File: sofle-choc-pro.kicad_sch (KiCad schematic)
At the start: 198 parts, among them J1 Connector, USB-TYPE-C-16P, J2 Connector, USB-TYPE-C-16P, J3 OLED 128x32 / nice!view, SW1 BOOT, SW10 F0, SW11 F1, SW12 F2, SW13 F3, SW14 F4, SW15 F5, SW16 F6 Choc/EC11, SW2 RESET, SW20 N0, SW21 N1, SW22 N2, SW23 N3, SW24 N4, SW25 N5, SW30 T0, SW31 T1, SW32 T2, SW33 T3, SW34 T4, SW35 T5, SW40 H0, SW41 H1, SW42 H2, SW43 H3, SW44 H4, SW45 H5, SW50 B0, SW51 B1, SW52 B2, SW53 B3, SW54 B4, SW55 B5, SW60 TH0, SW61 TH1, SW62 TH2, SW63 TH3, SW64 TH4, SW65 TH5 Choc/EC11, U1 RP2040, U2 USBLC6-2P6, U3 W25Q128JVPIQ, U4 USBLC6-2P6, U5 AP2112K-3.3, U6 SN74LV1T34DBVR, X1 ABM8-272-T3

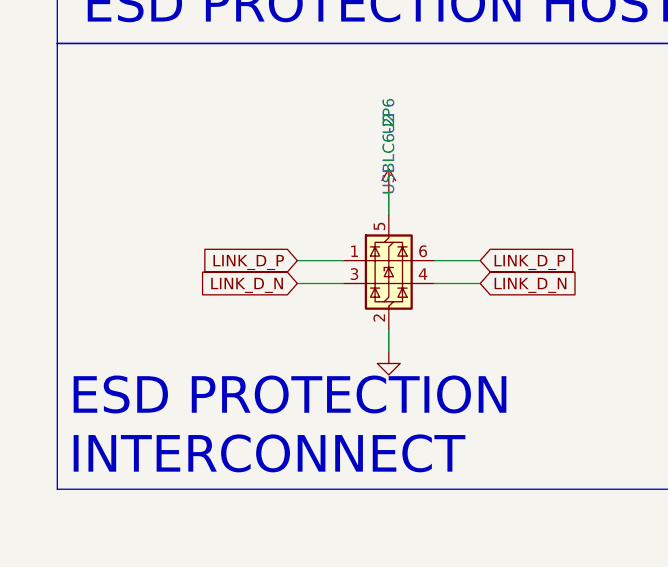
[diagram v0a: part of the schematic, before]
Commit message: fix(pcb): drop the dead link d- pad and exempt the esd fan-out
The link between halves is one-wire serial, so D- stops at the ESD array.
Both of its pads carried the net, which left KiCad asking for copper between
two pins the chip already joins inside. Now only the pad the connector
reaches is wired, and the other is a no-connect.

- U2 pin 3 disconnected in the schematic and on the board: four fewer
  unconnected items, and no more phantom pad-to-pad link
- D+/D- spacing rule now skips U4's courtyard as well as J1's and U1's,
  since the ESD array's two data pins sit 2.3 mm apart and set the gap

Also carries the USB and link routing done in KiCad since the last commit.

ERC 0 errors. DRC 0 errors, 0 parity issues. One skew flag remains on the
host pair (0.23 mm), to even out once that pair is finished.
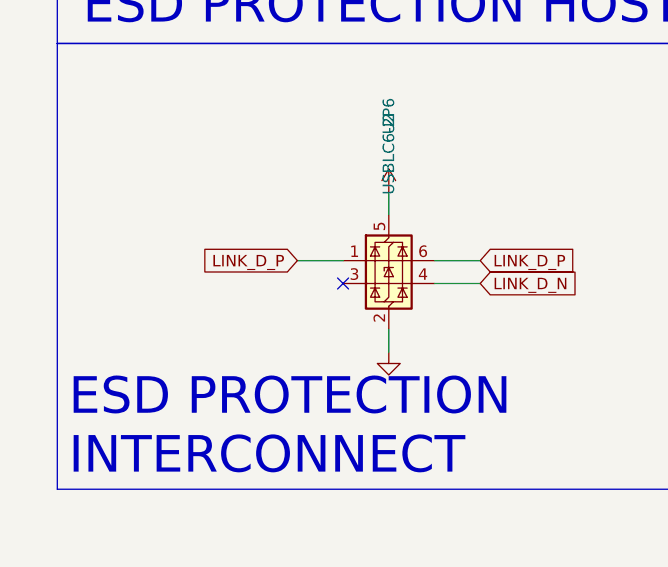
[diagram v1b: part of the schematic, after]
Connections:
- net LINK_D_N: no longer U2.3 (I/O2)
- no-connect marks 14 -> 15
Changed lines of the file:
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@@
 	(wire
 		(pts
-			(xy 45.72 269.24) (xy 40.64 269.24)
-		)
-		(stroke
-			(width 0)
-			(type default)
-		)
-	)
-	(wire
-		(pts
 			(xy 546.1 162.56) (xy 543.56 162.56)
 		)
@@
 		)
 	)
-	(global_label "LINK_D_N"
-		(shape input)
-		(at 40.64 269.24 180)
-		(effects
-			(font
-				(size 1.27 1.27)
-			)
-			(justify right)
-		)
-		(property "Intersheetrefs" "${INTERSHEET_REFS}"
-			(at 40.64 269.24 0)
-			(hide yes)
-			(show_name no)
-			(do_not_autoplace no)
-			(effects
-				(font
-					(size 1.27 1.27)
-				)
-			)
-		)
-	)
 	(global_label "LED_D23"
 		(shape bidirectional)
@@
 	)
 	(embedded_fonts no)
+	(no_connect
+		(at 45.72 269.24)
+	)
 )

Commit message: feat(pcb): route all power through the inner planes
Every power and ground pad is now connected, through a short stub to a
via beside the pad into the In1 and In2 planes, so the outer layers stay
free for signals.

- USB pair joined through U4: U2 and U4 use a project SOT-563 footprint
  that declares pins 1/6 and 3/4 as bonded, as ST's USBLC6-2 datasheet
  routes them, so D+/D- flow through the package
- VBUS runs 0.5 mm straight from J1 to F1; the D1 to U4 +5V trunk that
  blocked it is gone, and F1 to D1 widens to 0.5 mm
- +5V vias at D1/C18, U4, U2, U5, C20, F2, U6/C30 and every LED; each LED
  cap also gets a GND stitching via
- LINK_VBUS runs from J2 to F2, J2's two VBUS pads joined by an In1 strip;
  LINK_VBUS joins the Power5V class
- R10 moves beside the VBUS run so sense stays short; GP13 exits by a via
- J3 pin 3 takes +3.3V from an In1 branch; JP1's +3.3V logic tie runs
  0.2 mm on F.Cu down the right edge
- Two cap vias that sat within 0.1 mm of their pads get short stubs

Checks: DRC 0 errors, parity 0, ERC 0; nothing unconnected on power or
GND (179 signal items left, the GP13 via dangles until GP13 is routed).
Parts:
- U2, U4: footprint Package_TO_SOT_SMD:SOT-563 -> my-soffle:SOT-563_USBLC6-2P6
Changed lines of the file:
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@@
 			)
 		)
-		(property "Footprint" "Package_TO_SOT_SMD:SOT-563"
+		(property "Footprint" "my-soffle:SOT-563_USBLC6-2P6"
 			(at 60.96 217.17 0)
 			(hide yes)
@@
 			)
 		)
-		(property "Footprint" "Package_TO_SOT_SMD:SOT-563"
+		(property "Footprint" "my-soffle:SOT-563_USBLC6-2P6"
 			(at 60.96 266.7 0)
 			(hide yes)

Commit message: feat(pcb): start the led chain at the encoders and route columns 4-5
The LED data chain now runs R15, LED16, LED65, the thumbs, column 5 up
and column 4 down, so it no longer detours across column 5 to reach the
upper encoder. Columns 4 and 5 are routed by hand on the new order.

- Chain order picked by scoring every order on pad-to-pad length and
  crossings: 663 mm instead of 719 mm, no hop crosses a foreign key
  cell except LED63 to LED55 around SW2
- Only LED_D0 to LED_D8 were reassigned (9 LEDs); the routed tail from
  LED62 on is unchanged
- LED_D3 to LED_D14 routed, plus reworked GP22, GP24 and matrix nets

ERC: 0 errors. DRC: 0 errors, 0 parity, 29 unconnected. Known issues
to fix next: LED35/45/55 GND pads sealed off by the new data routes,
8 data vias touching their pads, a dangling GP22 via.
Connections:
- net LED_D0: now also LED16.2 (DIN); no longer LED65.2 (DIN)
- net LED_D1: now also LED16.4 (DOUT), LED65.2 (DIN); no longer LED64.2 (DIN), LED65.4 (DOUT)
- net LED_D2: now also LED64.2 (DIN), LED65.4 (DOUT); no longer LED63.2 (DIN), LED64.4 (DOUT)
- net LED_D3: now also LED63.2 (DIN), LED64.4 (DOUT); no longer LED55.2 (DIN), LED63.4 (DOUT)
- net LED_D4: now also LED55.2 (DIN), LED63.4 (DOUT); no longer LED45.2 (DIN), LED55.4 (DOUT)
- net LED_D5: now also LED45.2 (DIN), LED55.4 (DOUT); no longer LED35.2 (DIN), LED45.4 (DOUT)
- net LED_D6: now also LED35.2 (DIN), LED45.4 (DOUT); no longer LED25.2 (DIN), LED35.4 (DOUT)
- net LED_D7: now also LED25.2 (DIN), LED35.4 (DOUT); no longer LED15.2 (DIN), LED25.4 (DOUT)
- net LED_D8: now also LED15.2 (DIN), LED25.4 (DOUT); no longer LED15.4 (DOUT), LED16.2 (DIN)
- net LED_D9: now also LED15.4 (DOUT); no longer LED16.4 (DOUT)
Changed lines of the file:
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@@
 		)
 	)
-	(global_label "LED_D4"
+	(global_label "LED_D5"
 		(shape bidirectional)
 		(at 576.58 237.49 0)
@@
 		)
 	)
-	(global_label "LED_D9"
+	(global_label "LED_D1"
 		(shape bidirectional)
 		(at 444.5 273.05 0)
@@
 		)
 	)
-	(global_label "LED_D1"
+	(global_label "LED_D2"
 		(shape bidirectional)
 		(at 408.94 240.03 180)
@@
 		)
 	)
-	(global_label "LED_D6"
+	(global_label "LED_D7"
 		(shape bidirectional)
 		(at 708.66 237.49 0)
@@
 		)
 	)
-	(global_label "LED_D0"
+	(global_label "LED_D1"
 		(shape bidirectional)
 		(at 342.9 240.03 180)
@@
 		)
 	)
-	(global_label "LED_D7"
+	(global_label "LED_D8"
 		(shape bidirectional)
 		(at 774.7 237.49 0)
@@
 		)
 	)
-	(global_label "LED_D8"
+	(global_label "LED_D0"
 		(shape bidirectional)
 		(at 408.94 275.59 180)
@@
 		)
 	)
-	(global_label "LED_D3"
+	(global_label "LED_D4"
 		(shape bidirectional)
 		(at 541.02 240.03 180)
@@
 		)
 	)
-	(global_label "LED_D2"
+	(global_label "LED_D3"
 		(shape bidirectional)
 		(at 444.5 237.49 0)
@@
 		)
 	)
-	(global_label "LED_D6"
+	(global_label "LED_D7"
 		(shape bidirectional)
 		(at 739.14 240.03 180)
@@
 		)
 	)
-	(global_label "LED_D4"
+	(global_label "LED_D5"
 		(shape bidirectional)
 		(at 607.06 240.03 180)
@@
 		)
 	)
-	(global_label "LED_D5"
+	(global_label "LED_D6"
 		(shape bidirectional)
 		(at 673.1 240.03 180)
@@
 		)
 	)
-	(global_label "LED_D1"
+	(global_label "LED_D2"
 		(shape bidirectional)
 		(at 378.46 237.49 0)
@@
 		)
 	)
-	(global_label "LED_D8"
+	(global_label "LED_D9"
 		(shape bidirectional)
 		(at 378.46 273.05 0)
@@
 		)
 	)
-	(global_label "LED_D5"
+	(global_label "LED_D6"
 		(shape bidirectional)
 		(at 642.62 237.49 0)
@@
 		)
 	)
-	(global_label "LED_D7"
+	(global_label "LED_D8"
 		(shape bidirectional)
 		(at 342.9 275.59 180)
@@
 		)
 	)
-	(global_label "LED_D3"
+	(global_label "LED_D4"
 		(shape bidirectional)
 		(at 510.54 237.49 0)
@@
 		)
 	)
-	(global_label "LED_D2"
+	(global_label "LED_D3"
 		(shape bidirectional)
 		(at 474.98 240.03 180)

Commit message: feat(pcb): re-route the controller column and drop nice!view support
The inner column between U1 and the encoders is fully routed. The
display jumpers are gone and the GPIOs follow the order the lines leave
U1, so the column routes without crossings.

- OLED on I2C1 (SDA GP6, SCL GP7) on a 4-pin J3; nice!view CS and
  JP2/JP3 removed (QMK has no nice!view driver)
- SW16 encoder on GP13/GP14, VBUS sense on GP9; GP8, GP11, GP15-17 free
- East pins run as a ribbon through the lanes beside J2's shell legs;
  the boot line follows the east edge to SW1
- JP1 on the front by U1, R11 beside R10, R12/R13 pull-ups under J3
- In1 +3.3V island reaches J3 through a real finger, not a 0.5 mm strip
- Crystal, C5/C6 and TESTEN grounds no longer sealed off; XTAL_OUT
  clearance to C6 fixed

Under the hood: south of J3 is routed by the ribbon router; the rest is
hand-placed geometry checked with DRC. Backup of the old version: branch
backup/with-niceview-jumpers.

ERC: 0 errors. DRC: 0 errors, 0 unconnected, 0 parity.
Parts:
- removed JP2: SCL OLED=1-2 VIEW=2-3, Jumper:SolderJumper-3_P1.3mm_Open_RoundedPad1.0x1.5mm_NumberLabels, symbol Jumper:SolderJumper_3_Open
- removed JP3: SDA OLED=1-2 VIEW=2-3, Jumper:SolderJumper-3_P1.3mm_Open_RoundedPad1.0x1.5mm_NumberLabels, symbol Jumper:SolderJumper_3_Open
- J3: value OLED 128x32 / nice!view -> OLED 128x32; footprint Connector_PinHeader_2.54mm:PinHeader_1x05_P2.54mm_Vertical -> Connector_PinHeader_2.54mm:PinHeader_1x04_P2.54mm_Vertical; symbol Connector_Generic:Conn_01x05 -> Connector_Generic:Conn_01x04
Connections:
- net DISP_SCL is gone; now on net GP6: J3.4 (Pin_4)
- net +3.3V: now also J3.2 (Pin_2); no longer J3.3 (Pin_3)
- net GND: now also J3.1 (Pin_1); no longer J3.2 (Pin_2)
- net GP13: now also SW16.A; no longer R10.2, R11.1
- net GP14: now also SW16.B
- net GP7: now also J3.3 (Pin_3), R13.2; no longer SW16.A
- net GP9: now reaches U1.12 (GPIO9)
- net GP9: now also R10.2, R11.1
- net GP6: now reaches U1.8 (GPIO6)
- net GP6: now also R12.2
- removed net DISP_SDA: J3.5 (Pin_5)
- net GP11: no longer names the net of U1.14 (GPIO11)
- net GP11: no longer J3.1 (Pin_1)
- net GP15: no longer names the net of U1.18 (GPIO15)
- net GP16: no longer names the net of U1.27 (GPIO16)
- net GP16: no longer R12.2
- net GP17: no longer names the net of U1.28 (GPIO17)
- net GP17: no longer R13.2
- net GP8: no longer names the net of U1.11 (GPIO8)
- net GP8: no longer SW16.B
- no-connect marks 15 -> 18
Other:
- moved on the sheet: F2, J2, R16

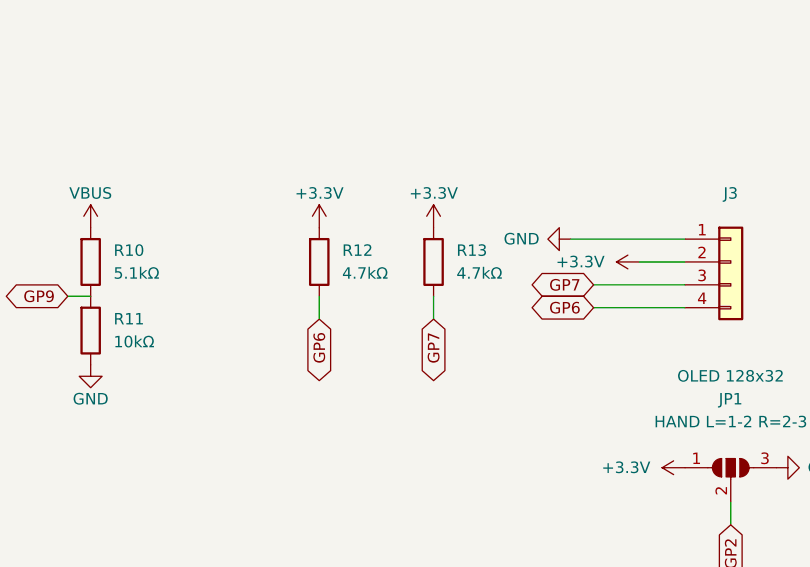
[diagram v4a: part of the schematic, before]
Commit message: fix(pcb): mirror J3 for the OLED module and clear the silkscreen
J3 now matches the 0.91 inch OLED module soldered face up and running
north: west to east it reads SDA, SCL, VCC, GND, like the module's own
header (JLCPCB C5248081, splitkb, Keycapsss). The old order would have
powered the module backwards.

- J3 1x04 rotated 180 degrees; SDA (GP6) and SCL (GP7) re-routed to its
  west pins under J3, +3.3V island reshaped round the new VCC pin
- R12/R13 removed: the module carries its own 4.7k I2C pull-ups
- Plate display opening centred on the module and clearing the glass
  by 0.5 mm (3.0 to 34.0 mm past the pins); key points unchanged
- Reference designators hidden on the silkscreen; outlines, pin-1 and
  polarity marks and the HOST/LINK labels kept
- GND via between J2's legs marked free so a zone refill cannot re-net
  it to the In1 +5V plane

ERC: 0 errors. DRC: 0 errors, 0 unconnected, 0 parity.
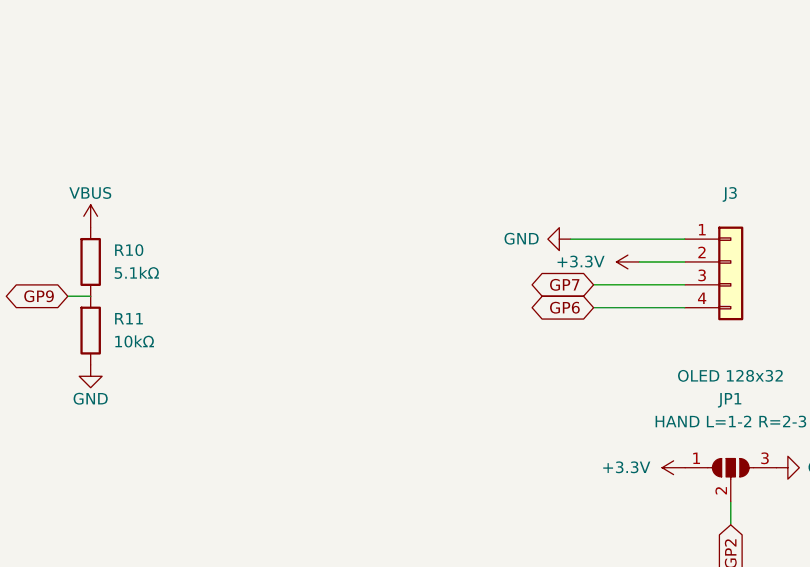
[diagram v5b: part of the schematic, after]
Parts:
- removed R12, R13: 4.7kΩ, PCM_JLCPCB:R_0402, symbol PCM_JLCPCB-Resistors:0402,4.7kΩ
